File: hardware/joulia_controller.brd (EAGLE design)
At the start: 32.1 x 61 mm, 27 parts, among them IC1 LM2902D, IC2 LM2902D, U1 MMBT2222ALT1G, U2 MMBT2222ALT1G

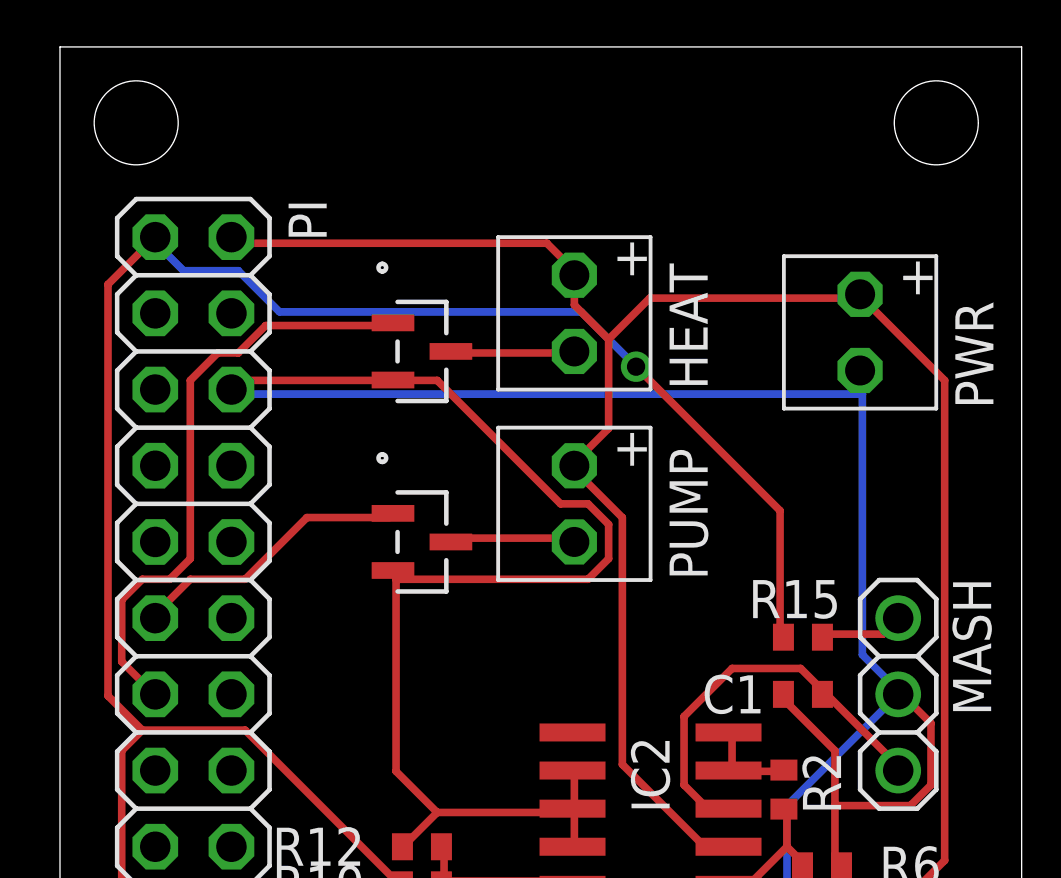
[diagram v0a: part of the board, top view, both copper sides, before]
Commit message: Increasing power trace width and adding input resistors to transistors.
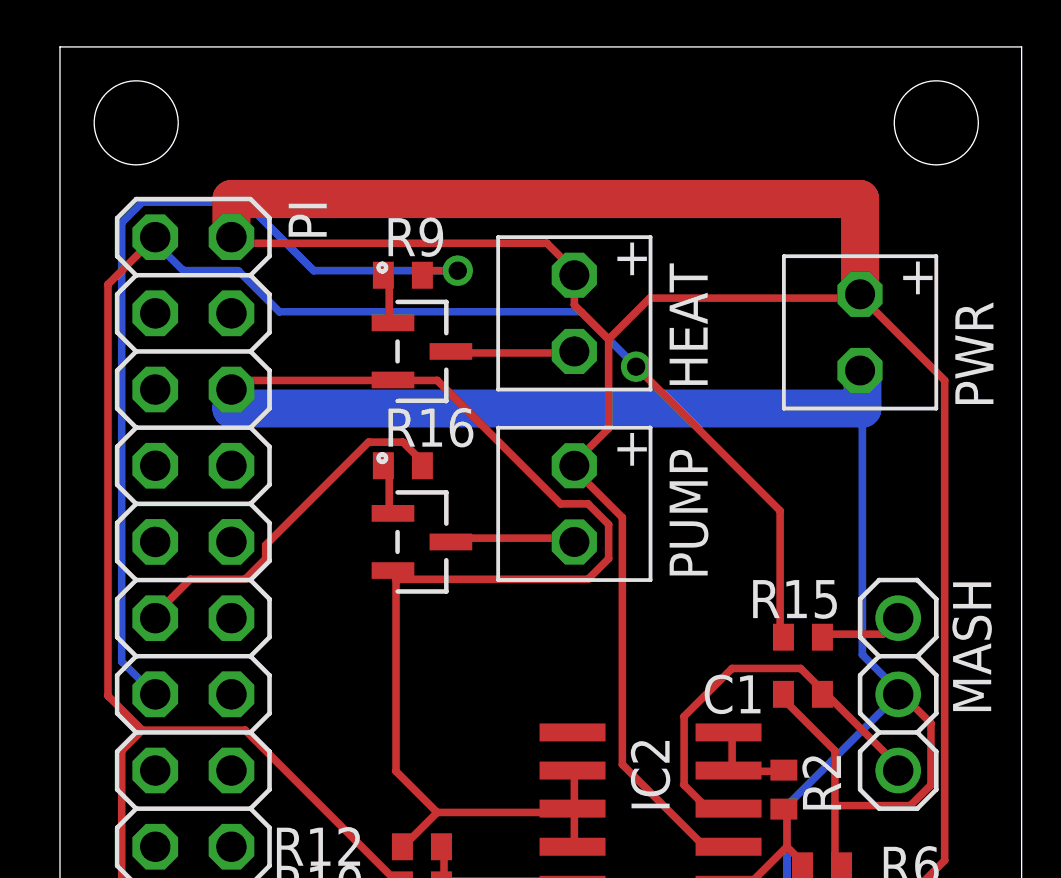
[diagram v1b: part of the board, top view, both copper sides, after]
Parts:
- added R16, R9: 1K, resistor:R0402
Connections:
- new net N$15: R9.1, U1.1
- new net N$16: R16.1, U2.1
- net HEOUT: now also R9.2; no longer U1.1
- net PPOUT: now also R16.2; no longer U2.1
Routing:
- net +5V: track 95.2 -> 120.6 mm
- net HEOUT: track 20.0 -> 29.9 mm, vias 0 -> 1
- net PPOUT: track 9.44 -> 12.1 mm
- net GND: track 176.1 -> 178.1 mm
- net N$15: track 0.00 -> 1.77 mm
- net N$16: track 0.00 -> 1.76 mm
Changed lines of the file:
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@@
 <?xml version="1.0" encoding="utf-8"?>
 <!DOCTYPE eagle SYSTEM "eagle.dtd">
-<eagle version="7.2.0">
+<eagle version="8.0.1">
 <drawing>
 <settings>
@@
 <attribute name="NAME" x="23.495" y="15.875" size="1.27" layer="25" rot="R180"/>
 </element>
+<element name="R9" library="resistor" package="R0402" value="1K" x="11.43" y="53.34" smashed="yes">
+<attribute name="NAME" x="10.795" y="53.975" size="1.27" layer="25"/>
+</element>
+<element name="R16" library="resistor" package="R0402" value="1K" x="11.43" y="46.99" smashed="yes">
+<attribute name="NAME" x="10.795" y="47.625" size="1.27" layer="25"/>
+</element>
 </elements>
 <signals>
@@
 <wire x1="25.8318" y1="33.8328" x2="26.05" y2="33.655" width="0.254" layer="1"/>
 <wire x1="24.003" y1="39.3192" x2="24.115" y2="39.37" width="0.254" layer="1"/>
-<wire x1="26.7462" y1="40.6908" x2="26.7462" y2="49.3776" width="0.254" layer="16"/>
-<wire x1="26.7462" y1="49.3776" x2="26.7462" y2="50.0634" width="0.254" layer="16"/>
+<wire x1="26.7462" y1="40.6908" x2="26.7462" y2="48.895" width="0.254" layer="16"/>
+<wire x1="26.7462" y1="48.895" x2="26.7462" y2="50.0634" width="0.254" layer="16"/>
 <wire x1="27.8892" y1="39.5478" x2="26.7462" y2="40.6908" width="0.254" layer="16"/>
 <wire x1="26.7462" y1="50.0634" x2="26.67" y2="50.165" width="0.254" layer="16"/>
@@
 <wire x1="24.2316" y1="35.6616" x2="24.2316" y2="18.288" width="0.254" layer="16"/>
 <wire x1="27.94" y1="39.37" x2="24.2316" y2="35.6616" width="0.254" layer="16"/>
-<wire x1="26.7462" y1="49.3776" x2="5.715" y2="49.3776" width="0.254" layer="16"/>
-<wire x1="5.715" y1="49.3776" x2="5.715" y2="49.53" width="0.254" layer="16"/>
+<wire x1="5.715" y1="49.53" x2="5.715" y2="49.3776" width="0.254" layer="16"/>
 <via x="16.002" y="18.288" extent="1-16" drill="0.6096"/>
 <via x="18.5166" y="16.002" extent="1-16" drill="0.6096"/>
+<wire x1="26.67" y1="50.165" x2="26.7462" y2="50.165" width="1.27" layer="16"/>
+<wire x1="26.7462" y1="50.165" x2="26.7462" y2="48.895" width="1.27" layer="16"/>
+<wire x1="26.7462" y1="48.895" x2="5.715" y2="48.895" width="1.27" layer="16"/>
+<wire x1="5.715" y1="48.895" x2="5.715" y2="49.53" width="1.27" layer="16"/>
 </signal>
 <signal name="N$4">
@@
 <wire x1="16.2306" y1="54.4068" x2="5.715" y2="54.4068" width="0.254" layer="1"/>
 <wire x1="17.145" y1="53.4924" x2="16.2306" y2="54.4068" width="0.254" layer="1"/>
-<wire x1="5.715" y1="54.4068" x2="5.715" y2="54.61" width="0.254" layer="1"/>
+<wire x1="5.715" y1="54.61" x2="5.715" y2="54.4068" width="0.254" layer="1"/>
 <wire x1="17.145" y1="53.4924" x2="17.145" y2="53.34" width="0.254" layer="1"/>
 <wire x1="29.4894" y1="33.8328" x2="20.574" y2="24.9174" width="0.254" layer="1"/>
@@
 <wire x1="26.7462" y1="52.578" x2="29.4894" y2="49.8348" width="0.254" layer="1"/>
 <wire x1="26.7462" y1="52.578" x2="26.67" y2="52.705" width="0.254" layer="1"/>
+<wire x1="26.67" y1="52.705" x2="26.67" y2="55.88" width="1.27" layer="1"/>
+<wire x1="26.67" y1="55.88" x2="5.715" y2="55.88" width="1.27" layer="1"/>
+<wire x1="5.715" y1="55.88" x2="5.715" y2="54.61" width="1.27" layer="1"/>
 </signal>
 <signal name="+3V3">
@@
 </signal>
 <signal name="HEOUT">
-<contactref element="U1" pad="1"/>
 <contactref element="PI" pad="13"/>
-<wire x1="6.858" y1="51.6636" x2="10.9728" y2="51.6636" width="0.254" layer="1"/>
-<wire x1="5.9436" y1="50.7492" x2="6.858" y2="51.6636" width="0.254" layer="1"/>
-<wire x1="5.2578" y1="50.7492" x2="5.9436" y2="50.7492" width="0.254" layer="1"/>
-<wire x1="4.3434" y1="49.8348" x2="5.2578" y2="50.7492" width="0.254" layer="1"/>
-<wire x1="4.3434" y1="43.8912" x2="4.3434" y2="49.8348" width="0.254" layer="1"/>
-<wire x1="3.6576" y1="43.2054" x2="4.3434" y2="43.8912" width="0.254" layer="1"/>
-<wire x1="2.7432" y1="43.2054" x2="3.6576" y2="43.2054" width="0.254" layer="1"/>
-<wire x1="2.0574" y1="42.5196" x2="2.7432" y2="43.2054" width="0.254" layer="1"/>
-<wire x1="2.0574" y1="40.4622" x2="2.0574" y2="42.5196" width="0.254" layer="1"/>
-<wire x1="2.9718" y1="39.5478" x2="2.0574" y2="40.4622" width="0.254" layer="1"/>
-<wire x1="10.9728" y1="51.6636" x2="11.0998" y2="51.7525" width="0.254" layer="1"/>
-<wire x1="2.9718" y1="39.5478" x2="3.175" y2="39.37" width="0.254" layer="1"/>
+<contactref element="R9" pad="2"/>
+<wire x1="13.2588" y1="53.4924" x2="12.1158" y2="53.4924" width="0.254" layer="1"/>
+<wire x1="8.4582" y1="53.4924" x2="13.2588" y2="53.4924" width="0.254" layer="16"/>
+<wire x1="6.1722" y1="55.7784" x2="8.4582" y2="53.4924" width="0.254" layer="16"/>
+<wire x1="2.7432" y1="55.7784" x2="6.1722" y2="55.7784" width="0.254" layer="16"/>
+<wire x1="2.0574" y1="55.0926" x2="2.7432" y2="55.7784" width="0.254" layer="16"/>
+<wire x1="2.0574" y1="40.4622" x2="2.0574" y2="55.0926" width="0.254" layer="16"/>
+<wire x1="2.9718" y1="39.5478" x2="2.0574" y2="40.4622" width="0.254" layer="16"/>
+<wire x1="12.1158" y1="53.4924" x2="12.08" y2="53.34" width="0.254" layer="1"/>
+<wire x1="2.9718" y1="39.5478" x2="3.175" y2="39.37" width="0.254" layer="16"/>
+<via x="13.2588" y="53.4924" extent="1-16" drill="0.6096"/>
 </signal>
 <signal name="PPOUT">
-<contactref element="U2" pad="1"/>
 <contactref element="PI" pad="11"/>
-<wire x1="8.2296" y1="45.2628" x2="10.9728" y2="45.2628" width="0.254" layer="1"/>
-<wire x1="6.1722" y1="43.2054" x2="8.2296" y2="45.2628" width="0.254" layer="1"/>
+<contactref element="R16" pad="2"/>
+<wire x1="11.8872" y1="47.3202" x2="11.8872" y2="47.0916" width="0.254" layer="1"/>
+<wire x1="11.43" y1="47.7774" x2="11.8872" y2="47.3202" width="0.254" layer="1"/>
+<wire x1="10.287" y1="47.7774" x2="11.43" y2="47.7774" width="0.254" layer="1"/>
+<wire x1="6.858" y1="44.3484" x2="10.287" y2="47.7774" width="0.254" layer="1"/>
+<wire x1="6.858" y1="43.8912" x2="6.858" y2="44.3484" width="0.254" layer="1"/>
+<wire x1="6.1722" y1="43.2054" x2="6.858" y2="43.8912" width="0.254" layer="1"/>
 <wire x1="4.3434" y1="43.2054" x2="6.1722" y2="43.2054" width="0.254" layer="1"/>
 <wire x1="3.2004" y1="42.0624" x2="4.3434" y2="43.2054" width="0.254" layer="1"/>
-<wire x1="10.9728" y1="45.2628" x2="11.0998" y2="45.4025" width="0.254" layer="1"/>
+<wire x1="11.8872" y1="47.0916" x2="12.08" y2="46.99" width="0.254" layer="1"/>
 <wire x1="3.2004" y1="42.0624" x2="3.175" y2="41.91" width="0.254" layer="1"/>
 </signal>
+<signal name="N$15">
+<contactref element="U1" pad="1"/>
+<contactref element="R9" pad="1"/>
+<wire x1="10.9728" y1="51.8922" x2="10.9728" y2="53.2638" width="0.254" layer="1"/>
+<wire x1="10.9728" y1="53.2638" x2="10.78" y2="53.34" width="0.254" layer="1"/>
+<wire x1="10.9728" y1="51.8922" x2="11.0998" y2="51.7525" width="0.254" layer="1"/>
+</signal>
+<signal name="N$16">
+<contactref element="U2" pad="1"/>
+<contactref element="R16" pad="1"/>
+<wire x1="10.9728" y1="45.4914" x2="10.9728" y2="46.863" width="0.254" layer="1"/>
+<wire x1="10.9728" y1="46.863" x2="10.78" y2="46.99" width="0.254" layer="1"/>
+<wire x1="10.9728" y1="45.4914" x2="11.0998" y2="45.4025" width="0.254" layer="1"/>
+</signal>
 </signals>
